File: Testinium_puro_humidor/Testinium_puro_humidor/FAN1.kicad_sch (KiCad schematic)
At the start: 0 parts

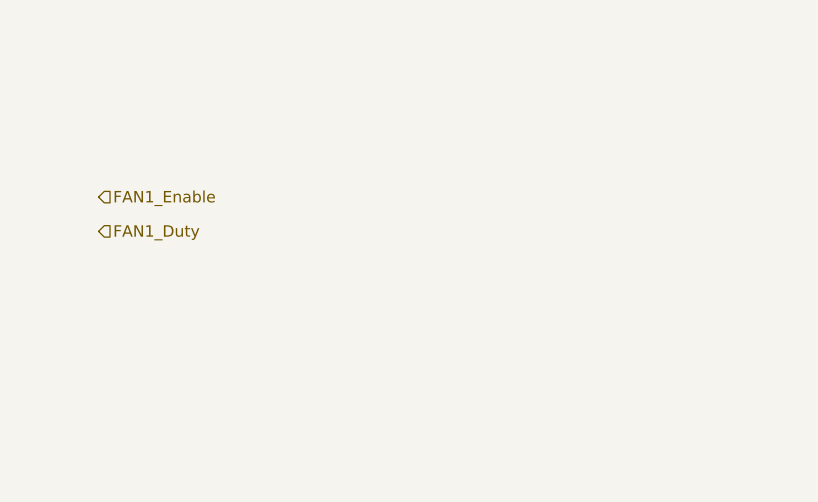
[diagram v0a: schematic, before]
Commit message: fan , uv led ,regülator devresi eklendi. piezo ve sarj devresi kaldi
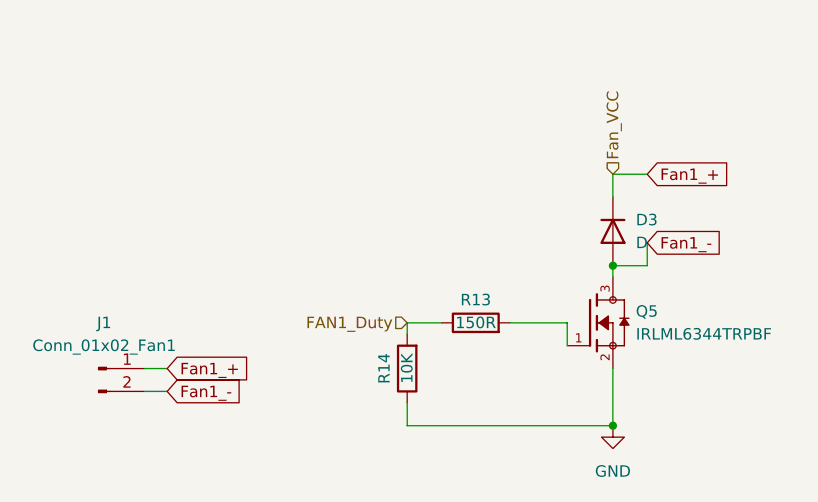
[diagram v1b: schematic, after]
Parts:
- added D3: D, symbol Device:D
- added J1: Conn_01x02_Fan1, Connector_JST:JST_EH_B2B-EH-A_1x02_P2.50mm_Vertical, symbol Connector:Conn_01x02_Pin
- added Q5: IRLML6344TRPBF, baraysan:TRANS_IRLML6344TRPBF, symbol BARAYSAN:IRLML6344TRPBF
- added R13: 150R, symbol Device:R
- added R14: 10K, symbol Device:R
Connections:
- net FAN1_Duty: now also R13.1, R14.2
- new net: Q5.1, R13.2
- new net Fan1_+: D3.1 (K), J1.1 (Pin_1)
- new net Fan1_-: D3.2 (A), J1.2 (Pin_2), Q5.3
- new net GND: Q5.2, R14.1

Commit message: sematik tamamlandi
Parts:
- added R25: 0R, Resistor_SMD:R_0603_1608Metric, symbol Device:R
- D3: footprint (none) -> Diode_SMD:D_SMA
- R13, R14: footprint (none) -> Resistor_SMD:R_0805_2012Metric
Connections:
- net Fan1_+: now also R25.1
- new net Fan_VCC: R25.2
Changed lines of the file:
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@@
 	)
 	(junction
-		(at 87.63 36.83)
+		(at 87.63 27.94)
 		(diameter 0)
 		(color 0 0 0 0)
 	)
+	(junction
+		(at 87.63 38.1)
+		(diameter 0)
+		(color 0 0 0 0)
+	)
 	(wire
 		(pts
@@
 	(wire
 		(pts
-			(xy 87.63 26.67) (xy 91.44 26.67)
-		)
-		(stroke
-			(width 0)
-			(type default)
-		)
-	)
-	(wire
-		(pts
-			(xy 91.44 36.83) (xy 87.63 36.83)
-		)
-		(stroke
-			(width 0)
-			(type default)
-		)
-	)
-	(wire
-		(pts
-			(xy 87.63 29.21) (xy 87.63 26.67)
+			(xy 91.44 38.1) (xy 87.63 38.1)
+		)
+		(stroke
+			(width 0)
+			(type default)
+		)
+	)
+	(wire
+		(pts
+			(xy 87.63 29.21) (xy 87.63 27.94)
+		)
+		(stroke
+			(width 0)
+			(type default)
+		)
+	)
+	(wire
+		(pts
+			(xy 87.63 27.94) (xy 91.44 27.94)
 		)
 		(stroke
@@
 	(wire
 		(pts
-			(xy 91.44 34.29) (xy 91.44 36.83)
+			(xy 91.44 34.29) (xy 91.44 38.1)
 		)
 		(stroke
@@
 	(global_label "Fan1_+"
 		(shape input)
-		(at 91.44 26.67 0)
+		(at 91.44 27.94 0)
 		(fields_autoplaced yes)
 		(effects
@@
 		)
 		(property "Intersheetrefs" "${INTERSHEET_REFS}"
-			(at 101.5613 26.67 0)
+			(at 101.5613 27.94 0)
 			(effects
 				(font
@@
 	(hierarchical_label "Fan_VCC"
 		(shape input)
-		(at 87.63 26.67 90)
+		(at 87.63 20.32 90)
 		(effects
 			(font
@@
 			)
 		)
-		(property "Footprint" ""
+		(property "Footprint" "Diode_SMD:D_SMA"
 			(at 87.63 33.02 0)
 			(effects
@@
 	(symbol
 		(lib_id "Device:R")
+		(at 87.63 24.13 180)
+		(unit 1)
+		(exclude_from_sim no)
+		(in_bom yes)
+		(on_board yes)
+		(dnp no)
+		(property "Reference" "R25"
+			(at 85.09 24.13 90)
+			(effects
+				(font
+					(size 1.27 1.27)
+				)
+			)
+		)
+		(property "Value" "0R"
+			(at 87.63 24.13 90)
+			(effects
+				(font
+					(size 1.27 1.27)
+				)
+			)
+		)
+		(property "Footprint" "Resistor_SMD:R_0603_1608Metric"
+			(at 89.408 24.13 90)
+			(effects
+				(font
+					(size 1.27 1.27)
+				)
+				(hide yes)
+			)
+		)
+		(property "Datasheet" "~"
+			(at 87.63 24.13 0)
+			(effects
+				(font
+					(size 1.27 1.27)
+				)
+				(hide yes)
+			)
+		)
+		(property "Description" "Resistor"
+			(at 87.63 24.13 0)
+			(effects
+				(font
+					(size 1.27 1.27)
+				)
+				(hide yes)
+			)
+		)
+		(property "HHH" ""
+			(at 87.63 24.13 0)
+			(effects
+				(font
+					(size 1.27 1.27)
+				)
+				(hide yes)
+			)
+		)
+		(pin "1"
+		)
+		(pin "2"
+		)
+		(instances
+			(project "Testinium_puro_humidor"
+				(path "/eaf24445-473d-4e1b-a90d-ef2c4a02e74f/fef5f3e3-3725-4a70-ae5b-3162558f79bf"
+					(reference "R25")
+					(unit 1)
+				)
+			)
+		)
+	)
+	(symbol
+		(lib_id "Device:R")
 		(at 72.39 43.18 90)
 		(unit 1)
@@
 			)
 		)
-		(property "Footprint" ""
+		(property "Footprint" "Resistor_SMD:R_0805_2012Metric"
 			(at 72.39 44.958 90)
 			(effects
@@
 			)
 		)
-		(property "Footprint" ""
+		(property "Footprint" "Resistor_SMD:R_0805_2012Metric"
 			(at 66.548 48.26 90)
 			(effects
